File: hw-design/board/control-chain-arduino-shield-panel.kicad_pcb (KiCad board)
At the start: 2 copper layers, 139.7 x 165 mm, 270 parts, among them J1 CC_INPUT, J2 CC_OUTPUT, P1 Power, P10 Power, P11 Analog, P12 Digital, P13 Digital, P2 Analog, P3 Digital, P4 Digital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

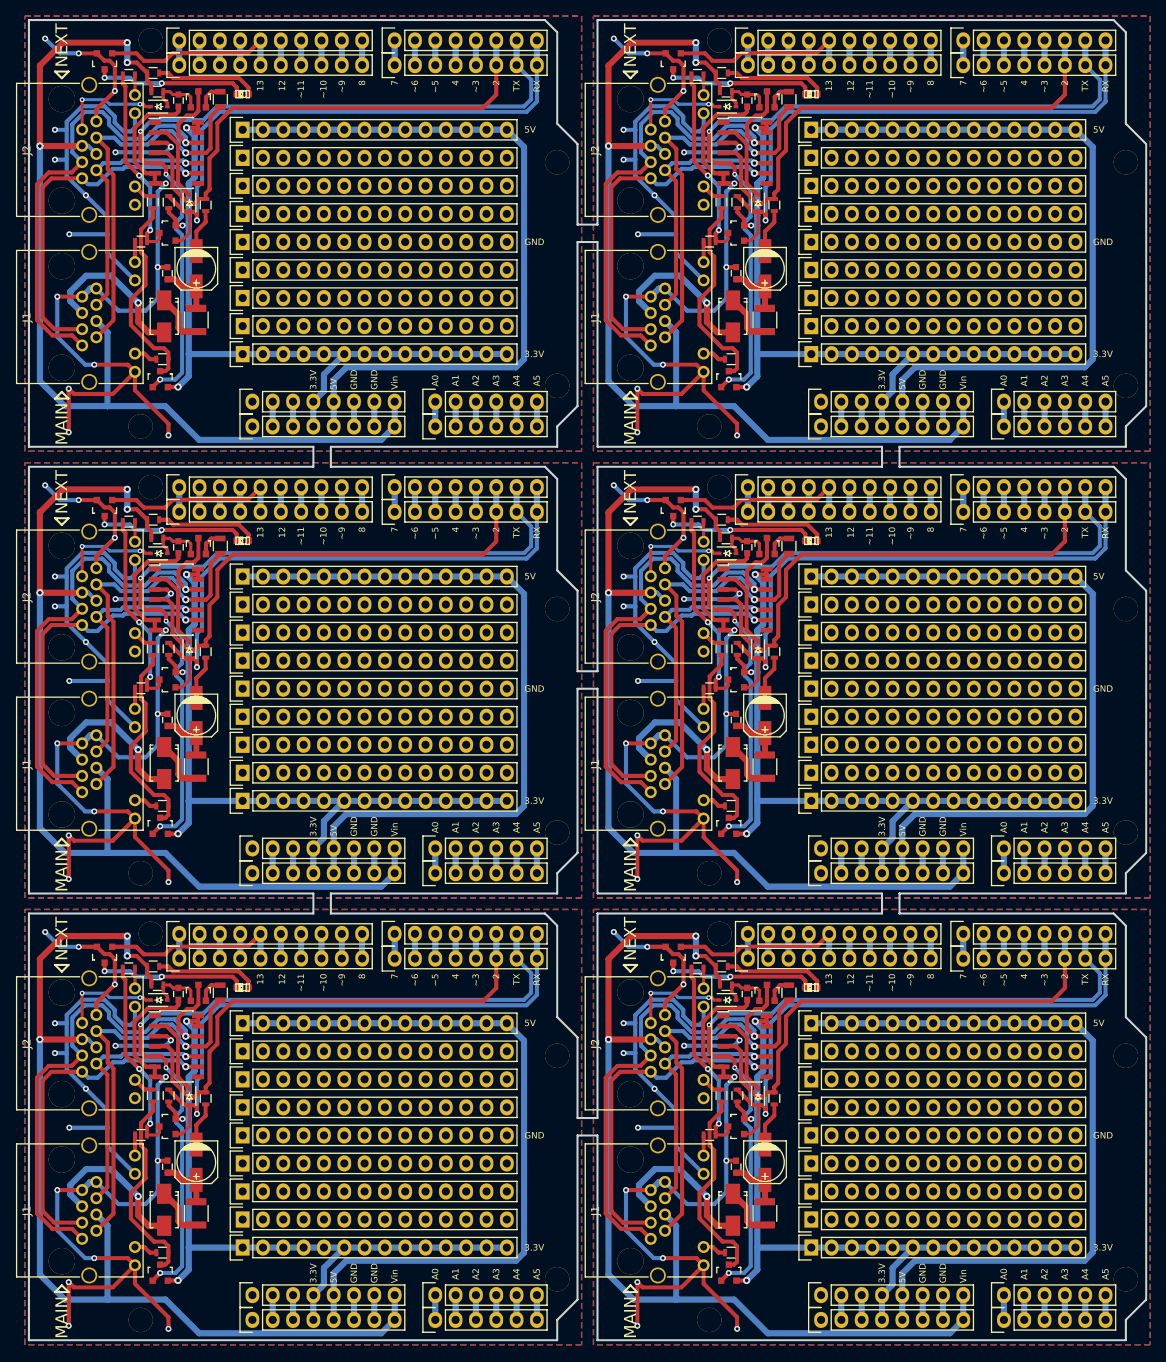
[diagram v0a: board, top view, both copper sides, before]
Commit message: fixing user led voltage
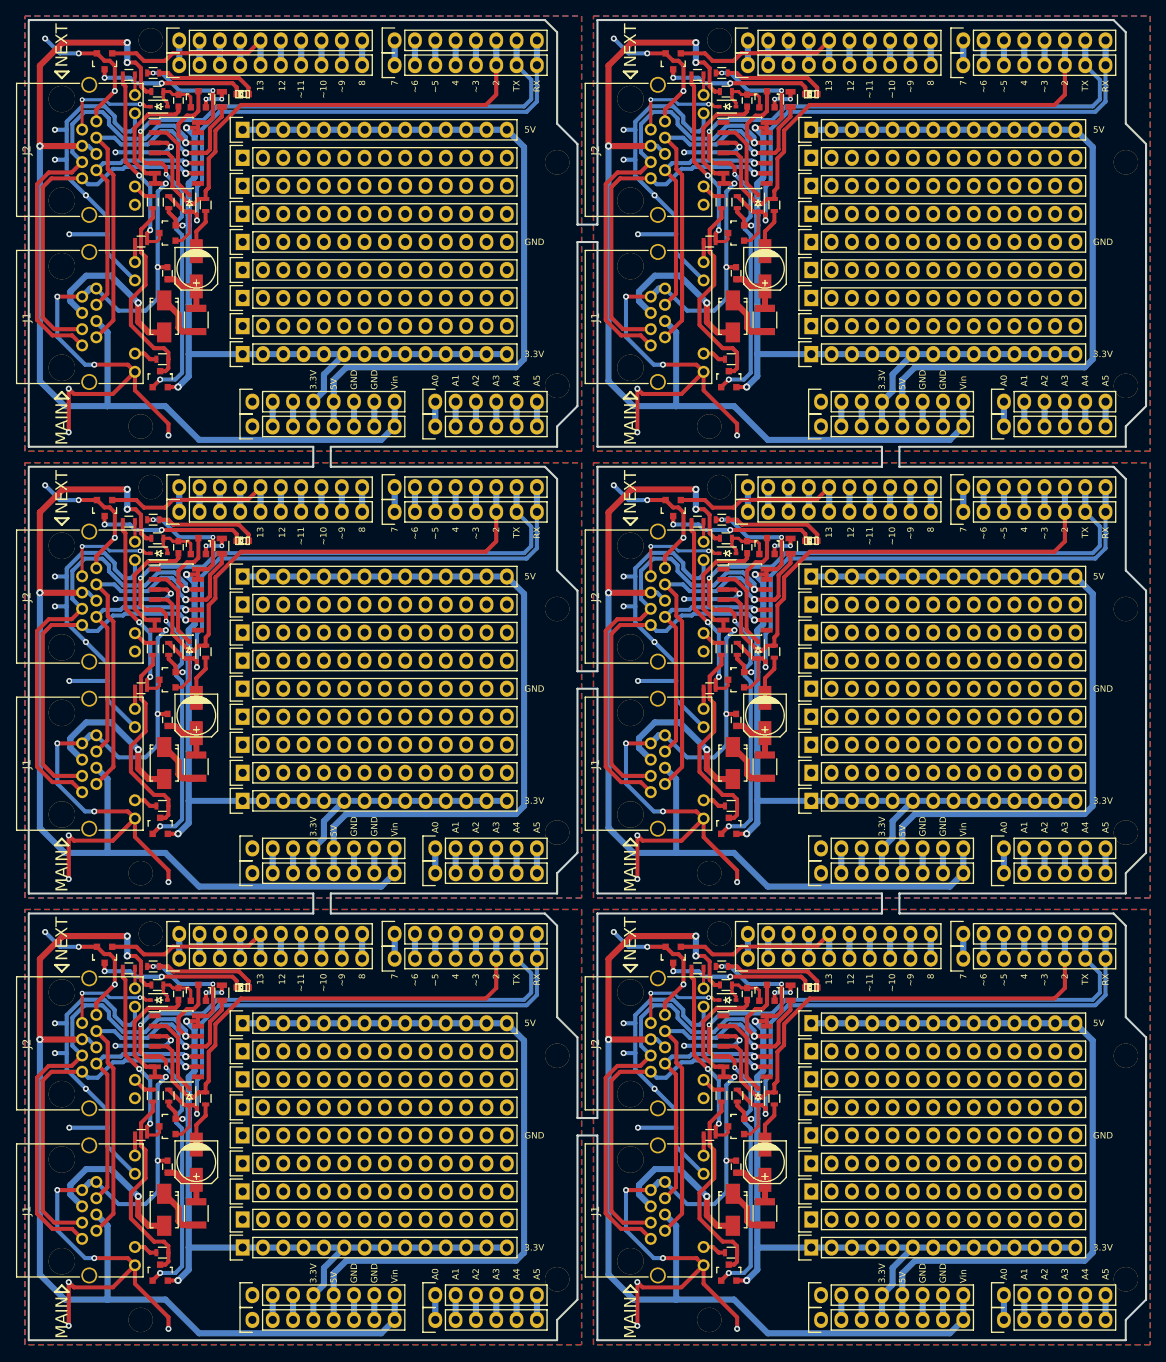
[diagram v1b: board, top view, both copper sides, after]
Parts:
- removed the R9 at (107.7, 134.3)
- removed the R9 at (107.7, 78.4)
- removed the R9 at (107.7, 22.6)
- removed the R9 at (36.6, 134.3)
- removed the R9 at (36.6, 78.4)
- added R9: 100R, Resistors_SMD:R_0805, F.Cu at (107.9, 134.3)
- added R9: 100R, Resistors_SMD:R_0805, F.Cu at (107.9, 78.5)
- added R9: 100R, Resistors_SMD:R_0805, F.Cu at (107.9, 22.6)
- added R9: 100R, Resistors_SMD:R_0805, F.Cu at (36.8, 134.3)
- added R9: 100R, Resistors_SMD:R_0805, F.Cu at (36.8, 78.5)
- R1 (x6): value 1K -> 330R
- moved R9 0.19 mm to (36.8, 22.6)
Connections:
- R1 pad 1: +12V -> +3V3 (x6)
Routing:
- net +3V3: track 553.6 -> 641.4 mm, vias 18 -> 30
- net Net-(Q4-Pad2): track 20.1 -> 23.6 mm, vias 0 -> 12
- net IO2: track 387.8 -> 385.3 mm
- net +12V: track 779.4 -> 781.2 mm
- net RS485_RX-: track 298.2 -> 298.8 mm
